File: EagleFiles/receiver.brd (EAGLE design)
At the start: 100 x 80 mm, 9 parts, among them IC1 MEGA8-AI

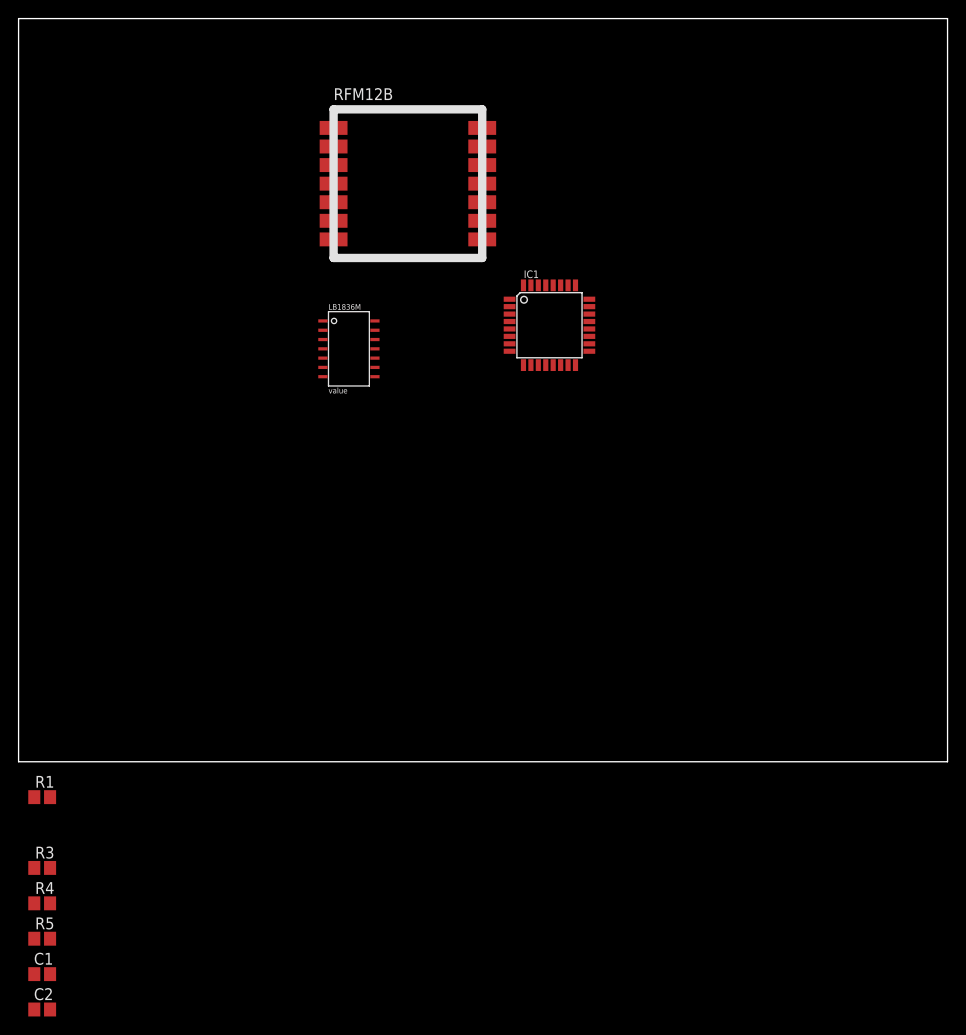
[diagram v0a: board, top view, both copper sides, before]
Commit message: Further development of the schematic and board
Schematic finalized, added a pinheader for programming and corrected
wiring errors. Board largely designed, including pads to solder the
motor and servo wires to.
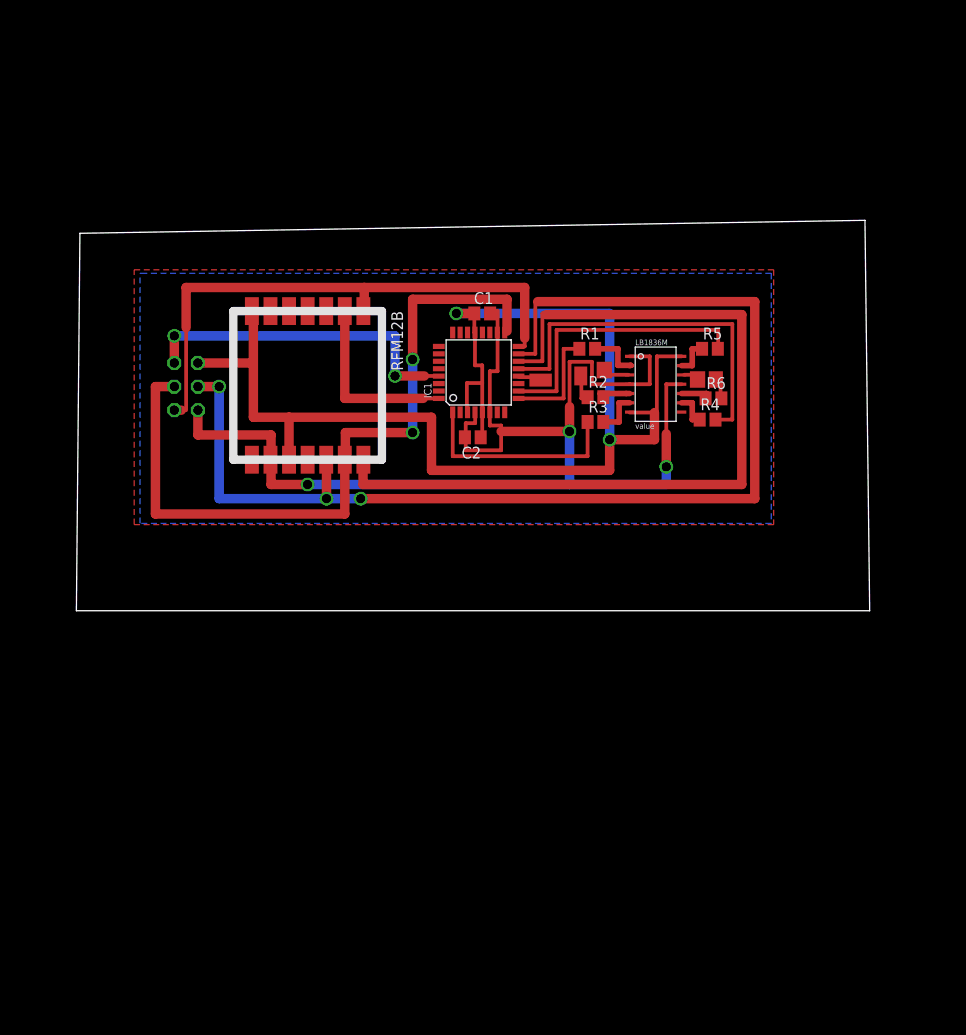
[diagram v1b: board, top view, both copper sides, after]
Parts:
- added JP1: ISP, pinhead:2X03
- added R2, R6: 10R, resistor:R2012
- C1: value (none) -> 0.10 uF
- C2: value (none) -> 0.1 uF
- R1, R3, R4, R5: value (none) -> 10k
- moved R5 95.9 mm to (74.4, 44.5)
- moved R4 88.6 mm to (74.2, 36.8)
- moved C1 85.5 mm to (49.9, 48.3)
- moved C2 77.1 mm to (48.9, 34.9), turned to 180 degrees
- moved R3 76.5 mm to (62.1, 36.6)
- moved R1 76.0 mm to (61.2, 44.5)
- moved LB1836M 33.2 mm to (68.6, 40.6)
- moved RFM12B 24.3 mm to (31.1, 40.5), turned to 270 degrees
- moved IC1 9.16 mm to (49.5, 41.9), turned to 90 degrees
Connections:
- new net N$14: LB1836M.OUT2, R2.2
- new net N$15: LB1836M.OUT4, R6.1
- new net N$20: IC1.29, JP1.5
- new net SERVO: IC1.12
- net GND: now also JP1.6
- net N$1: now also JP1.1
- net N$11: now also IC1.1; no longer IC1.24
- net N$12: now also IC1.13; no longer IC1.25
- net N$13: now also IC1.10; no longer IC1.26
- net N$2: now also JP1.4
- net N$3: now also JP1.3
- net N$7: now also IC1.9; no longer IC1.23
- net VCC: now also C2.2, JP1.2
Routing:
- net GND: track 0.00 -> 140.0 mm, vias 0 -> 2
- net VCC: track 0.00 -> 135.0 mm, vias 0 -> 3
- net N$2: track 0.00 -> 128.5 mm, vias 0 -> 3
- net N$4: track 0.00 -> 91.0 mm
- net N$3: track 0.00 -> 80.7 mm, vias 0 -> 2
- net N$1: track 0.00 -> 62.2 mm
- net N$12: track 0.00 -> 40.0 mm
- net N$20: track 0.00 -> 35.7 mm, vias 0 -> 2
- net N$13: track 0.00 -> 30.2 mm
- net N$11: track 0.00 -> 22.9 mm
- net N$5: track 0.00 -> 19.5 mm
- net N$7: track 0.00 -> 11.9 mm
- net N$6: track 0.00 -> 5.75 mm
- net N$8: track 0.00 -> 4.89 mm
- net N$10: track 0.00 -> 4.00 mm
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- added copper zone on layer 1, net GND
- added copper zone on layer 16, net GND
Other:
- board size 100 x 80 mm -> 85.4 x 42 mm

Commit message: Small changes to board
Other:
- board size 85.4 x 42 mm -> 85.9 x 42 mm
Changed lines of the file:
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@@
 <layer number="17" name="Pads" color="2" fill="1" visible="yes" active="yes"/>
 <layer number="18" name="Vias" color="2" fill="1" visible="yes" active="yes"/>
-<layer number="19" name="Unrouted" color="6" fill="1" visible="yes" active="yes"/>
-<layer number="20" name="Dimension" color="15" fill="1" visible="no" active="yes"/>
-<layer number="21" name="tPlace" color="7" fill="1" visible="yes" active="yes"/>
-<layer number="22" name="bPlace" color="7" fill="1" visible="yes" active="yes"/>
-<layer number="23" name="tOrigins" color="15" fill="1" visible="yes" active="yes"/>
-<layer number="24" name="bOrigins" color="15" fill="1" visible="yes" active="yes"/>
-<layer number="25" name="tNames" color="7" fill="1" visible="yes" active="yes"/>
-<layer number="26" name="bNames" color="7" fill="1" visible="yes" active="yes"/>
+<layer number="19" name="Unrouted" color="6" fill="1" visible="no" active="yes"/>
+<layer number="20" name="Dimension" color="15" fill="1" visible="yes" active="yes"/>
+<layer number="21" name="tPlace" color="7" fill="1" visible="no" active="yes"/>
+<layer number="22" name="bPlace" color="7" fill="1" visible="no" active="yes"/>
+<layer number="23" name="tOrigins" color="15" fill="1" visible="no" active="yes"/>
+<layer number="24" name="bOrigins" color="15" fill="1" visible="no" active="yes"/>
+<layer number="25" name="tNames" color="7" fill="1" visible="no" active="yes"/>
+<layer number="26" name="bNames" color="7" fill="1" visible="no" active="yes"/>
 <layer number="27" name="tValues" color="7" fill="1" visible="no" active="yes"/>
 <layer number="28" name="bValues" color="7" fill="1" visible="no" active="yes"/>
@@
 <layer number="43" name="vRestrict" color="2" fill="10" visible="no" active="yes"/>
 <layer number="44" name="Drills" color="7" fill="1" visible="no" active="yes"/>
-<layer number="45" name="Holes" color="7" fill="1" visible="no" active="yes"/>
+<layer number="45" name="Holes" color="7" fill="1" visible="yes" active="yes"/>
 <layer number="46" name="Milling" color="3" fill="1" visible="no" active="yes"/>
 <layer number="47" name="Measures" color="7" fill="1" visible="no" active="yes"/>
@@
 <board>
 <plain>
-<wire x1="6.223" y1="16.256" x2="91.618" y2="16.256" width="0" layer="20"/>
+<wire x1="5.715" y1="17.526" x2="91.618" y2="16.256" width="0" layer="20"/>
 <wire x1="91.618" y1="16.256" x2="91.11" y2="58.283" width="0" layer="20"/>
-<wire x1="91.11" y1="58.283" x2="6.604" y2="56.886" width="0" layer="20"/>
-<wire x1="6.604" y1="56.886" x2="6.223" y2="16.256" width="0" layer="20"/>
+<wire x1="91.11" y1="58.283" x2="6.096" y2="58.156" width="0" layer="20"/>
+<wire x1="6.096" y1="58.156" x2="5.715" y2="17.526" width="0" layer="20"/>
 <rectangle x1="72.263" y1="40.259" x2="73.914" y2="42.037" layer="1"/>
 <rectangle x1="74.295" y1="40.259" x2="75.819" y2="42.037" layer="1"/>
@@
 <rectangle x1="59.817" y1="40.513" x2="61.214" y2="42.545" layer="1"/>
 <rectangle x1="54.991" y1="40.386" x2="57.404" y2="41.783" layer="1"/>
+<hole x="15.24" y="49.657" drill="0.6"/>
+<hole x="73.533" y="33.274" drill="0.6"/>
+<hole x="18.034" y="31.242" drill="0.6"/>
 </plain>
 <attributes>
@@
 <wire x1="44.45" y1="31.369" x2="63.627" y2="31.369" width="1.016" layer="1"/>
 <wire x1="63.627" y1="31.369" x2="63.627" y2="34.671" width="1.016" layer="1"/>
-<polygon width="1.016" layer="1">
+<polygon width="1.016" layer="1" isolate="0.6096">
 <vertex x="12.446" y="52.959"/>
 <vertex x="81.28" y="52.959"/>
@@
 <vertex x="12.446" y="25.527"/>
 </polygon>
-<polygon width="1.016" layer="16">
+<polygon width="1.016" layer="16" isolate="0.4064">
 <vertex x="13.208" y="52.578"/>
 <vertex x="81.026" y="52.578"/>
@@
 <vertex x="13.081" y="52.578"/>
 </polygon>
+<wire x1="65.78" y1="37.592" x2="65.78" y2="37.64" width="0" layer="19" extent="1-1"/>
 </signal>
 <signal name="N$2">
